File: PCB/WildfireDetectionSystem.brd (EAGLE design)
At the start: 80 x 60 mm, 110 parts, among them IC1 STM32L476RGT6, J1 10118192-0001LF, J3 B4B-XH-A, J4 B5B-XH-A, J7 B4B-PH-K-S, J8 U.FL-R-SMT-1(10), J9 B2B-PH-K-S, SW1 434133025816, U1 BME280, U2 TPS63070RNMR, U3 NEO-6M-GPS, U4 TPS62142RGTT, U5 TPS61022RWUR, U6 LMR33630ADDA, U7 BQ24074RGTR, Y1 ABLS-8.000MHZ-B2-T, Y2 ECS-.327-12.5-12QS-TR

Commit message: pcbv2
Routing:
- net GND: track 222.0 -> 220.0 mm, vias 55 -> 54
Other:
- board text added: "Created by: Kevin Yu Jake Gilbert Manny Lemus Frank Xiao Aliston Ma UCSB 2026"
- board text removed: "Created by: Kevin Yu Jake Gilbert Manny Lemus Frank Xiao Aliston Ma"
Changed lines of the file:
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@@
 <text x="0.4" y="-17.3" size="1.778" layer="21">+</text>
 <text x="41.6" y="-7.2" size="1.778" layer="21">GPS</text>
-<text x="58.7" y="-14.6" size="1.27" layer="21">Created by:
+<text x="58.8" y="-16.2" size="1.27" layer="21">Created by:
 Kevin Yu
 Jake Gilbert
 Manny Lemus
 Frank Xiao
-Aliston Ma</text>
+Aliston Ma
+UCSB 2026</text>
 <text x="70.9" y="-15.9" size="0.6096" layer="21">        )
    (   ( ) )  )
@@
 <wire x1="8.2" y1="30.7" x2="6.6" y2="30.7" width="0.2032" layer="1"/>
 <via x="6.6" y="30.7" extent="1-16" drill="0.35"/>
-<wire x1="30.802" y1="11.897" x2="30.785" y2="11.88" width="0.2032" layer="1"/>
 <wire x1="36.081" y1="14.292" x2="36.615" y2="14.826" width="0.2032" layer="1"/>
 <wire x1="44.051" y1="9.342" x2="44.051" y2="7.535" width="0.2032" layer="1"/>
@@
 <wire x1="5.6" y1="-17.25" x2="7.2" y2="-15.65" width="0.2032" layer="1"/>
 <wire x1="7.2" y1="-15.65" x2="7.2" y2="-15.6" width="0.2032" layer="1"/>
-<wire x1="9.45" y1="-11.465" x2="9.434" y2="-11.449" width="0.2032" layer="1"/>
-<wire x1="9.434" y1="-11.449" x2="9.434" y2="-11.348825" width="0.2032" layer="1"/>
-<wire x1="10.95" y1="-3.25" x2="11" y2="-3.2" width="0.2032" layer="1"/>
-<via x="11" y="-3.2" extent="1-16" drill="0.35"/>
 <wire x1="5.25" y1="-9.7" x2="5.25" y2="-10.85" width="0.2032" layer="1"/>
 <wire x1="5.25" y1="-10.85" x2="5.4" y2="-11" width="0.2032" layer="1"/>
@@
 <wire x1="37.6" y1="-12.25" x2="38.1" y2="-12.75" width="0.2032" layer="1"/>
 <wire x1="38.1" y1="-12.75" x2="39.9" y2="-12.75" width="0.2032" layer="1"/>
-<wire x1="31.8907875" y1="-12.65" x2="32.2" y2="-12.65" width="0.2032" layer="1"/>
 <wire x1="31.75" y1="-9.1" x2="30.5" y2="-9.1" width="0.2032" layer="1"/>
 <via x="30.5" y="-9.1" extent="1-16" drill="0.35"/>
@@
 <wire x1="10.615" y1="-15" x2="10.8" y2="-15" width="0.2032" layer="1"/>
 <via x="10.8" y="-15" extent="1-16" drill="0.35"/>
-<wire x1="9.7" y1="-3.85" x2="10.35" y2="-3.85" width="0.2032" layer="1"/>
-<wire x1="11" y1="-3.2" x2="10.35" y2="-3.85" width="0.2032" layer="1"/>
 <contactref element="R23" pad="1"/>
 <wire x1="5.6" y1="-13.95" x2="5.25" y2="-14.3" width="0.1524" layer="1"/>
@@
 <wire x1="19.9160375" y1="-11.92581875" x2="19.525" y2="-11.92581875" width="0.2032" layer="1"/>
 <wire x1="20.29465625" y1="-11.5472" x2="19.9160375" y2="-11.92581875" width="0.2032" layer="1"/>
-<wire x1="20.025" y1="-13.7" x2="19.8278" y2="-13.5028" width="0.2032" layer="1"/>
+<wire x1="20.025" y1="-13.7" x2="19.9278" y2="-13.6028" width="0.2032" layer="1"/>
 <wire x1="19.29801875" y1="-12.4472" x2="19.29801875" y2="-12.1528" width="0.2032" layer="1"/>
-<wire x1="19.8278" y1="-13.5028" x2="19.8278" y2="-12.97698125" width="0.2032" layer="1"/>
-<wire x1="19.8278" y1="-12.97698125" x2="19.29801875" y2="-12.4472" width="0.2032" layer="1"/>
+<wire x1="19.9278" y1="-13.6028" x2="19.9278" y2="-13.07698125" width="0.2032" layer="1"/>
+<wire x1="19.9278" y1="-13.07698125" x2="19.29801875" y2="-12.4472" width="0.2032" layer="1"/>
 <wire x1="28.2" y1="-10.15" x2="27.6" y2="-10.75" width="0.2032" layer="1"/>
 <wire x1="27.6" y1="-10.75" x2="26.1" y2="-10.75" width="0.2032" layer="1"/>
@@
 <wire x1="10.8" y1="-5.65" x2="12.6" y2="-5.65" width="0.2032" layer="1"/>
 <wire x1="12.6" y1="-5.65" x2="12.7" y2="-5.55" width="0.2032" layer="1"/>
-<wire x1="10.8" y1="-5.65" x2="10.8" y2="-3.4" width="0.2032" layer="1"/>
-<wire x1="10.8" y1="-3.4" x2="11" y2="-3.2" width="0.2032" layer="1"/>
+<wire x1="10.8" y1="-5.65" x2="10.8" y2="-4.2" width="0.2032" layer="1"/>
 <wire x1="9.45" y1="-11.465" x2="9.45" y2="-10.85" width="0.2032" layer="1"/>
 <wire x1="8.35" y1="-9.75" x2="8.35" y2="-9.5" width="0.2032" layer="1"/>
@@
 <wire x1="19.525" y1="-10.175" x2="19.6" y2="-10.1" width="0.2032" layer="1"/>
 <via x="19.6" y="-10.1" extent="1-16" drill="0.35"/>
+<wire x1="10.45" y1="-3.85" x2="10.8" y2="-4.2" width="0.2032" layer="1"/>
+<wire x1="9.7" y1="-3.85" x2="10.45" y2="-3.85" width="0.2032" layer="1"/>
 </signal>
 <signal name="5V">
@@
 <wire x1="22.1" y1="0.8" x2="34" y2="0.8" width="0.3048" layer="1"/>
 <wire x1="39.9" y1="-11.05" x2="42.45" y2="-8.5" width="0.3048" layer="1"/>
-<wire x1="42.45" y1="-8.5" x2="63.5" y2="-8.5" width="0.3048" layer="1"/>
-<wire x1="73.7" y1="1.7" x2="75.4" y2="1.7" width="0.3048" layer="1"/>
+<wire x1="42.45" y1="-8.5" x2="50.9" y2="-8.5" width="0.3048" layer="1"/>
+<wire x1="61.1" y1="1.7" x2="75.4" y2="1.7" width="0.3048" layer="1"/>
 <wire x1="75.4" y1="1.7" x2="76.5" y2="2.8" width="0.3048" layer="1"/>
 <wire x1="76.5" y1="20.29" x2="70.19" y2="26.6" width="0.3048" layer="1"/>
 <wire x1="70.19" y1="26.6" x2="70.19" y2="34.7" width="0.3048" layer="1"/>
-<wire x1="63.5" y1="-8.5" x2="73.7" y2="1.7" width="0.3048" layer="1"/>
+<wire x1="50.9" y1="-8.5" x2="61.1" y2="1.7" width="0.3048" layer="1"/>
 <wire x1="76.5" y1="2.8" x2="76.5" y2="20.29" width="0.3048" layer="1"/>
 <contactref element="C3" pad="1"/>
@@
 <wire x1="33.625" y1="-14.3829125" x2="33.55" y2="-14.4" width="0.2032" layer="1"/>
 <wire x1="24.35" y1="-15.6" x2="24.15" y2="-15.6" width="0.2032" layer="1"/>
-<wire x1="24.15" y1="-15.6" x2="22.65" y2="-17.1" width="0.2032" layer="1"/>
-<wire x1="22.65" y1="-17.1" x2="22.7" y2="-17.05" width="0.2032" layer="1"/>
 <wire x1="33.625" y1="-11.35" x2="32.6" y2="-11.35" width="0.2032" layer="1"/>
 <wire x1="32.6" y1="-11.35" x2="32.2" y2="-10.95" width="0.2032" layer="1"/>
@@
 <wire x1="32.2" y1="-11.34855" x2="32.2" y2="-10.95" width="0.2032" layer="1"/>
 <wire x1="32.8778" y1="-12.02635" x2="32.2" y2="-11.34855" width="0.2032" layer="1"/>
-<wire x1="22.65" y1="-17.1" x2="24.15" y2="-18.6" width="0.2032" layer="1"/>
+<wire x1="22.65" y1="-17.1" x2="22.675" y2="-17.125" width="0.2032" layer="1"/>
+<wire x1="22.675" y1="-17.125" x2="24.15" y2="-18.6" width="0.2032" layer="1"/>
 <wire x1="29.4079125" y1="-18.6" x2="33.625" y2="-14.3829125" width="0.2032" layer="1"/>
 <wire x1="24.15" y1="-18.6" x2="29.4079125" y2="-18.6" width="0.2032" layer="1"/>
-<wire x1="22.65" y1="-17.1" x2="21.55" y2="-18.2" width="0.2032" layer="1"/>
-<wire x1="21.55" y1="-18.2" x2="11.7" y2="-18.2" width="0.2032" layer="1"/>
-<wire x1="11.7" y1="-18.2" x2="11.2" y2="-17.7" width="0.2032" layer="1"/>
+<wire x1="11.2" y1="-17.7" x2="11.7" y2="-18.2" width="0.2032" layer="1"/>
 <wire x1="11.2" y1="-17.7" x2="12" y2="-17.7" width="0.2032" layer="1"/>
 <wire x1="12.65" y1="-16.4" x2="12.65" y2="-16.15" width="0.2032" layer="1"/>
@@
 <wire x1="12.64855" y1="-13.2" x2="12.25" y2="-13.2" width="0.2032" layer="1"/>
 <wire x1="13.32635" y1="-13.8778" x2="12.64855" y2="-13.2" width="0.2032" layer="1"/>
+<wire x1="24.15" y1="-15.6" x2="22.65" y2="-17.1" width="0.2032" layer="1"/>
+<wire x1="21.6" y1="-18.2" x2="22.675" y2="-17.125" width="0.2032" layer="1"/>
+<wire x1="11.7" y1="-18.2" x2="21.6" y2="-18.2" width="0.2032" layer="1"/>
 </signal>
 <signal name="ILIM">

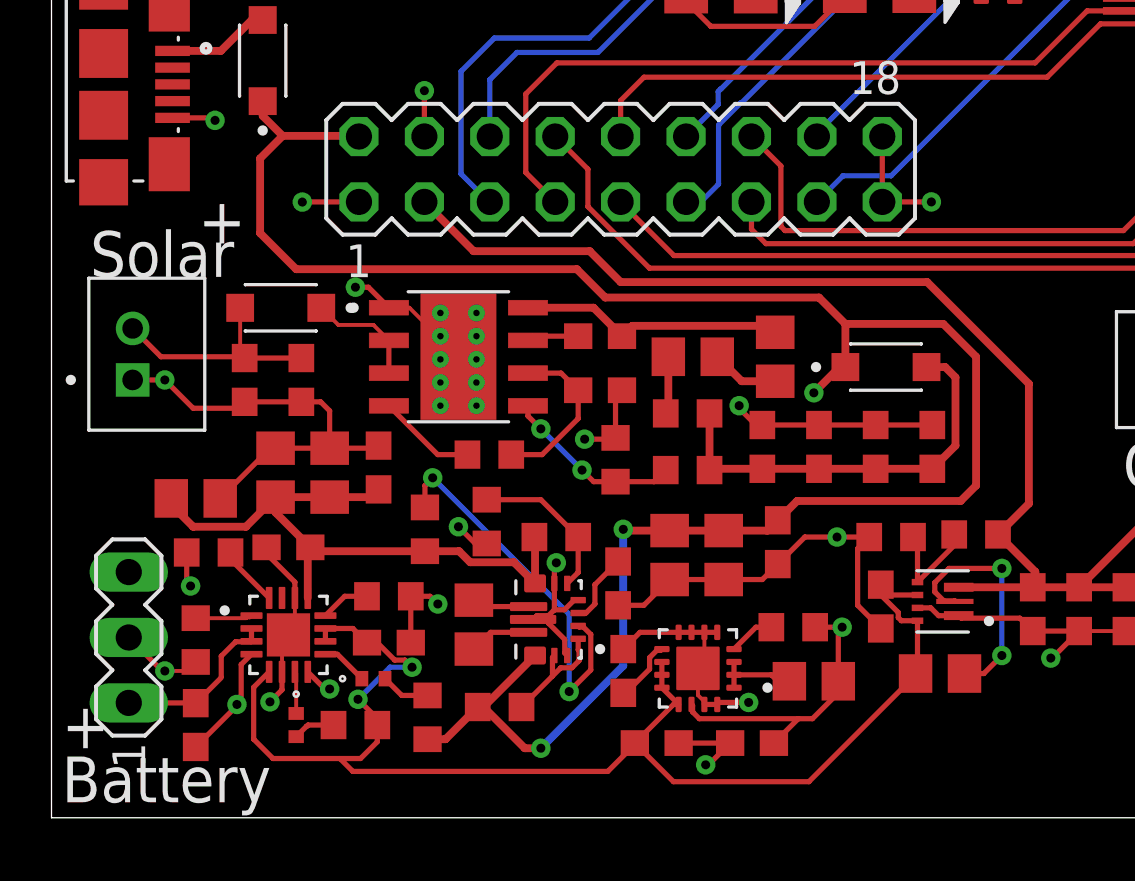
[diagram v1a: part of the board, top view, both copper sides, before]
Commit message: changed charging circuit to add buck/boost
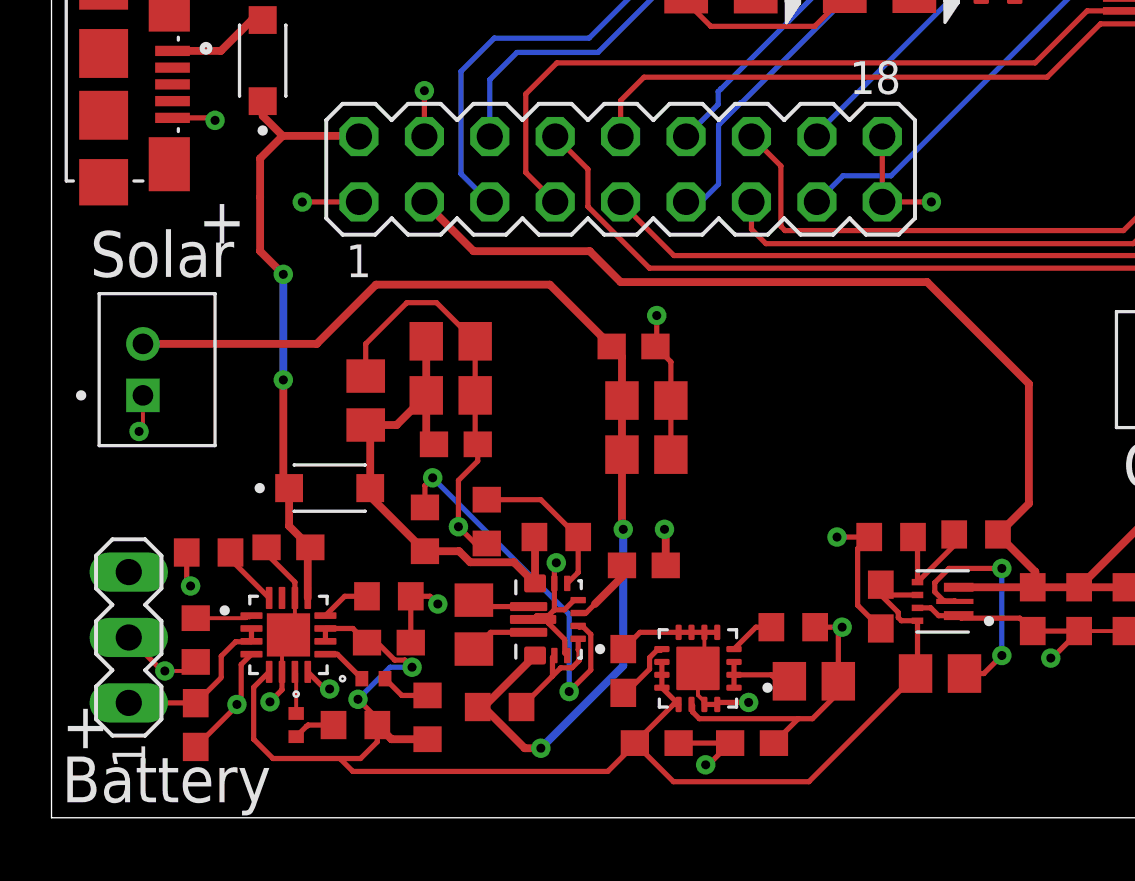
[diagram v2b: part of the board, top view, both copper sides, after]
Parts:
- removed C18, C26, C27, C28: 22uF, JLC PCB Basic Parts_loc:C0603
- removed C29: .1uF, JLC PCB Basic Parts_loc:C0603
- removed C30: 1uF, JLC PCB Basic Parts_loc:C0603
- removed C31: 220nF, JLC PCB Basic Parts_loc:C0603
- removed C32: 10uF, JLC PCB Basic Parts_loc:C0603
- removed D8: SS34LWH, SS34LWH:SODFL3718X102N
- removed J9: B2B-PH-K-S, B2B-PH-K-S:JST_B2B-PH-K-S
- removed L2: L_1R0_0805, JLC PCB Basic Parts_loc:R0805
- removed L5: L_4R7_0603, JLC PCB Basic Parts_loc:R0603
- removed L6: L_2R2_0805, JLC PCB Basic Parts_loc:R0805
- removed R17, R18: 100k, JLC PCB Basic Parts_loc:R0603
- removed R19: 24.9k, rcl:R0603
- removed U6: LMR33630ADDA, LMR33630ADDA:VREG_LM5017MR/NOPB
- added J5: B2B-PH-K-S, B2B-PH-K-S:JST_B2B-PH-K-S
- U2: value TPS63070RNMR -> TPS63070RNMT; device TPS63070RNMR:VREG_TPS63070RNMR -> TPS63070RNMT:VREG_TPS63070RNMT
- moved D9 22.1 mm to (10.8, -7.20)
- moved C5 9.44 mm to (22.6, -1.70), turned to 180 degrees
- moved C42 8.50 mm to (15.5, -1.50), turned to 0 degrees
- moved C41 7.62 mm to (12.2, -3.80), turned to 90 degrees
- moved C39 6.71 mm to (23.1, -3.80), turned to 0 degrees
- moved C40 5.58 mm to (15.5, -3.60), turned to 0 degrees
- moved C23 4.00 mm to (23.1, -5.90), turned to 0 degrees
- moved C4 3.13 mm to (15.7, -5.50), turned to 180 degrees
- moved C43 1.22 mm to (23.0, -10.2), turned to 0 degrees
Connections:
- removed net 5V_BUCK: C16.1, C4.2, C40.1, C41.1, C42.1, R24.2, R25.1, U2.7_8, U7.13
- removed net 5V_IN_SOLAR: C18.1, C26.1, C27.1, C28.1, D9.A, L5.1, R17.1
- removed net BOOT: C29.2, U6.7
- removed net FB: R17.2, R19.1, U6.5
- removed net N$1: L5.2, L6.1
- removed net N$15: D8.C, U6.2, U6.3
- removed net N$16: L2.2, L6.2
- removed net PG2: R18.1, U6.4
- removed net SW3: C29.1, L2.1, U6.8
- removed net VCC: C30.1, R18.2, U6.6
- new net 5V_SOLAR: C4.2, C40.1, C41.1, C42.1, D9.A, R24.2, R25.1, U2.7_8
- net 5V_IN: now also C16.1, U7.13; no longer C23.1, C39.1, C5.2, R16.2, R6.2, U2.12_13
- net GND: now also J5.1; no longer C18.2, C26.2, C27.2, C28.2, C30.2, C31.2, C32.2, J9.1, R19.2, U6.1, U6.9
- net SOLAR_IN: now also C23.1, C39.1, C5.2, J5.2, R6.2, U2.12_13; no longer C31.1, C32.1, D8.A, J9.2
- net SYS: now also R16.2
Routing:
- net 5V_IN: track 79.6 -> 23.9 mm, vias 3 -> 2
- net SOLAR_IN: track 9.05 -> 43.2 mm, vias 0 -> 2
- net 5V_BUCK: track 24.9 -> 0.00 mm
- net GND: track 220.0 -> 199.9 mm, vias 54 -> 43
- net 5V_SOLAR: track 0.00 -> 19.4 mm
- net 5V_IN_SOLAR: track 16.1 -> 0.00 mm
- net SW3: track 10.3 -> 0.00 mm
- net FB: track 6.99 -> 0.00 mm, vias 2 -> 0
- net VCC: track 6.51 -> 0.00 mm
- net N$15: track 4.42 -> 0.00 mm
- net PG2: track 3.83 -> 0.00 mm
- net N$16: track 2.64 -> 0.00 mm
- net N$1: track 2.24 -> 0.00 mm
- net SYS: track 53.1 -> 55.3 mm
- net BOOT: track 2.02 -> 0.00 mm

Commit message: inductor change
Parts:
- removed L8: L_1R0_0805, JLC PCB Basic Parts_loc:R0805
- added L2: DFE252012P-1R5M=P2, DFE252012P-1R5M_P2:INDC2520X120N
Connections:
- net N$19: now also L2.2; no longer L8.1
- net N$20: now also L2.1; no longer L8.2
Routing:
- net GND: track 199.9 -> 200.4 mm
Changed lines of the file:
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@@
 <attribute name="PROPERTIES" value="±1% 1/10W Thick Film Resistors 75V ±100ppm -55°C~+155°C 130kOhm 0603  ROHS" x="16.9" y="-8.5" size="1.778" layer="27" rot="R90" display="off"/>
-</element>
-<element name="L8" library="JLC PCB Basic Parts_loc" package="R0805" package3d_urn="urn:adsk.eagle:package:23553/2" value="L_1R0_0805" x="16.4" y="-12.5" smashed="yes" rot="R90">
-<attribute name="LCSC_DATASHEET" value="https://datasheet.lcsc.com/lcsc/2110081230_Sunlord-SDFL2012Q1R0KTF_C1042.pdf" x="16.4" y="-12.5" size="1.778" layer="27" rot="R90" display="off"/>
-<attribute name="LCSC_PART" value="C1042" x="16.4" y="-12.5" size="1.778" layer="27" rot="R90" display="off"/>
-<attribute name="LCSC_PRICE1_EUR" value="" x="16.4" y="-12.5" size="1.778" layer="27" rot="R90" display="off"/>
-<attribute name="LCSC_ROTATION_CCW" value="0" x="16.4" y="-12.5" size="1.778" layer="27" rot="R90" display="off"/>
-<attribute name="LCSC_STOCK" value="44995" x="16.4" y="-12.5" size="1.778" layer="27" rot="R90" display="off"/>
-<attribute name="PROPERTIES" value="ManuPN: SDFL2012Q1R0KTF 50mA 1uH ±10% 400mOhm 0805  ROHS" x="16.4" y="-12.5" size="1.778" layer="27" rot="R90" display="off"/>
 </element>
 <element name="J5" library="B2B-PH-K-S" package="JST_B2B-PH-K-S" value="B2B-PH-K-S" x="4.1" y="-2.6" smashed="yes" rot="R270">
@@
 <attribute name="PURCHASE-URL" value="https://www.snapeda.com/api/url_track_click_mouser/?unipart_id=473612&amp;manufacturer=JST Sales&amp;part_name=B2B-PH-K-S&amp;search_term=b2b-ph-k-s" x="4.1" y="-2.6" size="1.778" layer="27" rot="R270" display="off"/>
 <attribute name="SNAPEDA_LINK" value="https://www.snapeda.com/parts/B2B-PH-K-S/JST/view-part/?ref=snap" x="4.1" y="-2.6" size="1.778" layer="27" rot="R270" display="off"/>
+</element>
+<element name="L2" library="DFE252012P-1R5M_P2" package="INDC2520X120N" value="DFE252012P-1R5M=P2" x="16.071" y="-12.381" smashed="yes" rot="R270">
+<attribute name="AVAILABILITY" value="In Stock" x="16.071" y="-12.381" size="1.778" layer="27" rot="R270" display="off"/>
+<attribute name="CHECK_PRICES" value="https://www.snapeda.com/parts/DFE252012P-1R5M=P2/Murata+Electronics+North+America/view-part/?ref=eda" x="16.071" y="-12.381" size="1.778" layer="27" rot="R270" display="off"/>
+<attribute name="DESCRIPTION" value="                                                      Inductor with Inductance: 1.5uH Tol. +/-20%, Package: 1008 (2520)                                              " x="16.071" y="-12.381" size="1.778" layer="27" rot="R270" display="off"/>
+<attribute name="MF" value="Murata Electronics" x="16.071" y="-12.381" size="1.778" layer="27" rot="R270" display="off"/>
+<attribute name="MP" value="DFE252012P-1R5M=P2" x="16.071" y="-12.381" size="1.778" layer="27" rot="R270" display="off"/>
+<attribute name="PACKAGE" value="2520 Murata" x="16.071" y="-12.381" size="1.778" layer="27" rot="R270" display="off"/>
+<attribute name="PRICE" value="None" x="16.071" y="-12.381" size="1.778" layer="27" rot="R270" display="off"/>
+<attribute name="SNAPEDA_LINK" value="https://www.snapeda.com/parts/DFE252012P-1R5M=P2/Murata+Electronics+North+America/view-part/?ref=snap" x="16.071" y="-12.381" size="1.778" layer="27" rot="R270" display="off"/>
 </element>
 </elements>
@@
 <wire x1="5.25" y1="-10.85" x2="5.4" y2="-11" width="0.2032" layer="1"/>
 <via x="5.4" y="-11" extent="1-16" drill="0.35"/>
-<wire x1="14.7" y1="-11.4" x2="15" y2="-11.7" width="0.2032" layer="1"/>
-<wire x1="14.7" y1="-11.4" x2="13.95" y2="-11.4" width="0.2032" layer="1"/>
-<via x="15" y="-11.7" extent="1-16" drill="0.35"/>
+<wire x1="13.95" y1="-11.4" x2="13.95" y2="-11.35" width="0.2032" layer="1"/>
+<wire x1="13.95" y1="-11.35" x2="12.8" y2="-10.2" width="0.2032" layer="1"/>
+<via x="12.8" y="-10.2" extent="1-16" drill="0.35"/>
 <wire x1="25.85" y1="-15.6" x2="25.35" y2="-15.6" width="0.2032" layer="1"/>
 <wire x1="25.85" y1="-12.8" x2="25.35" y2="-12.8" width="0.2032" layer="1"/>
@@
 <contactref element="U7" pad="13"/>
 <contactref element="C16" pad="1"/>
-<wire x1="9.95" y1="-11.465" x2="9.95" y2="-9.6" width="0.3048" layer="1"/>
-<wire x1="9.95" y1="-9.6" x2="10.05" y2="-9.5" width="0.3048" layer="1"/>
-<wire x1="10" y1="-9.65" x2="9.95" y2="-9.6" width="0.3048" layer="1"/>
 <contactref element="D9" pad="C"/>
-<wire x1="10.05" y1="-9.5" x2="9.225" y2="-8.675" width="0.3048" layer="1"/>
 <wire x1="9.225" y1="-8.675" x2="9.225" y2="-7.2" width="0.3048" layer="1"/>
 <wire x1="9.225" y1="-7.2" x2="9" y2="-6.975" width="0.3048" layer="1"/>
@@
 <via x="9" y="1.1" extent="1-16" drill="0.35"/>
 <wire x1="9" y1="1.1" x2="8.1" y2="2" width="0.3048" layer="1"/>
-<wire x1="8.1" y1="2" x2="8.1" y2="4.1" width="0.3048" layer="1"/>
-<wire x1="8.1" y1="4.1" x2="8.1" y2="5.6" width="0.3048" layer="1"/>
+<wire x1="8.1" y1="2" x2="8.1" y2="5.6" width="0.3048" layer="1"/>
+<wire x1="9.95" y1="-11.465" x2="9.95" y2="-9.6" width="0.3048" layer="1"/>
+<wire x1="9.95" y1="-9.6" x2="10.05" y2="-9.5" width="0.3048" layer="1"/>
+<wire x1="10.05" y1="-9.5" x2="9.225" y2="-8.675" width="0.3048" layer="1"/>
 </signal>
 <signal name="PC14-OSC32-IN">
@@
 <signal name="N$19">
 <contactref element="U2" pad="11"/>
-<contactref element="L8" pad="1"/>
-<wire x1="18.525" y1="-12.8" x2="17.05" y2="-12.8" width="0.2032" layer="1"/>
-<wire x1="17.05" y1="-12.8" x2="16.4" y2="-13.45" width="0.2032" layer="1"/>
+<contactref element="L2" pad="2"/>
+<wire x1="18.525" y1="-12.8" x2="16.742" y2="-12.8" width="0.2032" layer="1"/>
+<wire x1="16.742" y1="-12.8" x2="16.071" y2="-13.471" width="0.2032" layer="1"/>
 </signal>
 <signal name="N$20">
 <contactref element="U2" pad="9"/>
-<contactref element="L8" pad="2"/>
-<wire x1="18.525" y1="-11.8" x2="16.65" y2="-11.8" width="0.2032" layer="1"/>
-<wire x1="16.65" y1="-11.8" x2="16.4" y2="-11.55" width="0.2032" layer="1"/>
+<contactref element="L2" pad="1"/>
+<wire x1="18.525" y1="-11.8" x2="16.58" y2="-11.8" width="0.2032" layer="1"/>
+<wire x1="16.58" y1="-11.8" x2="16.071" y2="-11.291" width="0.2032" layer="1"/>
 </signal>
 <signal name="N$23">

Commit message: pcbv2
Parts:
- D10, D9: value SS34LWH -> DSK34; device SS34LWH:SODFL3718X102N -> MDD_DSK34_LCSC_C41029:SOD-123_L2.8-W1.8-LS3.7-RD
- U$1: value 24LC32AT-I/SN -> 24LC32AT-I_SN; device 24LC32AT-I_SN:SOIC127P794X203-8N -> MICROCHIP_24LC32AT-I_SN_LCSC_C615715:SOIC-8_L4.9-W3.9-P1.27-LS6.0-BL
- moved D10 1.30 mm to (8.20, 8.10)
- moved D9 0.10 mm to (10.7, -7.20)
- moved U$1 0.10 mm to (27.5, 25.5), turned to 90 degrees
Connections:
- net 5V_IN: now also D10.1, D9.1; no longer D10.C, D9.C
- net 5V_IN_USB: now also D10.2; no longer D10.A
- net 5V_SOLAR: now also D9.2; no longer D9.A
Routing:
- net GND: track 200.4 -> 207.0 mm, vias 43 -> 42
- net GPS_SDA: track 4.81 -> 6.09 mm
- net GPS_SCL: track 7.91 -> 9.20 mm
- net 3V3: track 60.0 -> 61.3 mm
- net 5V_IN: track 23.8 -> 22.5 mm
